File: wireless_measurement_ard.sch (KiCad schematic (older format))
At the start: 22 parts, among them J1 Conn_01x08, SW1 SW_SPDT, U2 JDY-08, U3 MCP16415, U4 MAX9938, U5 MAX9938, U6 EFM8LB1x-QFP32

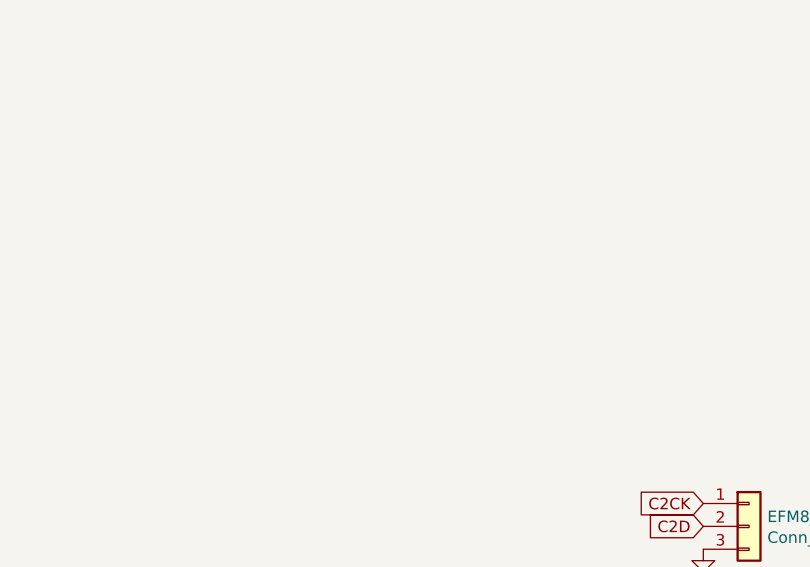
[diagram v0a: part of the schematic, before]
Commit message: update kicad to include holes
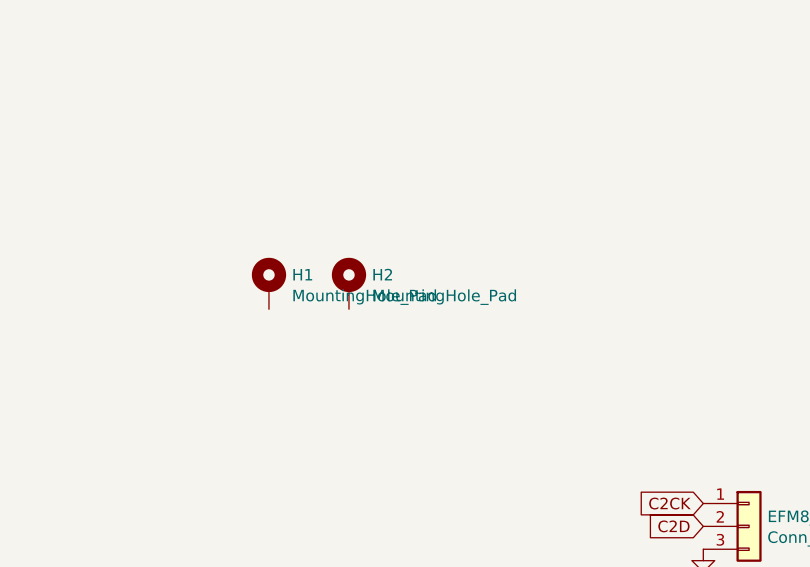
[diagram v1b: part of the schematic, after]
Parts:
- added H1, H2: MountingHole_Pad, MountingHole:MountingHole_2.2mm_M2_ISO7380_Pad, symbol Mechanical:MountingHole_Pad
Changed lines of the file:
@@
 Text GLabel 6200 4650 0    50   Input ~ 0
 VIN
+$Comp
+L Mechanical:MountingHole_Pad H1
+U 1 1 6108948B
+P 5550 2350
+F 0 "H1" H 5650 2399 50  0000 L CNN
+F 1 "MountingHole_Pad" H 5650 2308 50  0000 L CNN
+F 2 "MountingHole:MountingHole_2.2mm_M2_ISO7380_Pad" H 5550 2350 50  0001 C CNN
+F 3 "~" H 5550 2350 50  0001 C CNN
+	1    5550 2350
+	1    0    0    -1
+$EndComp
+$Comp
+L Mechanical:MountingHole_Pad H2
+U 1 1 61089F2F
+P 5900 2350
+F 0 "H2" H 6000 2399 50  0000 L CNN
+F 1 "MountingHole_Pad" H 6000 2308 50  0000 L CNN
+F 2 "MountingHole:MountingHole_2.2mm_M2_ISO7380_Pad" H 5900 2350 50  0001 C CNN
+F 3 "~" H 5900 2350 50  0001 C CNN
+	1    5900 2350
+	1    0    0    -1
+$EndComp
 $EndSCHEMATC

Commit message: update to fix VIO
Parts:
- added U1: EFM8LB1, Package_DFN_QFN:QFN-32-1EP_4x4mm_P0.4mm_EP2.9x2.9mm, symbol MCU_SiliconLabs:EFM8LB1
- U2: symbol jdy-08:JDY-08 -> wireless_measurement_ard-rescue:JDY-08-jdy-08
- U3: symbol gen_lib:MCP16415 -> wireless_measurement_ard-rescue:MCP16415-gen_lib
- U4, U5: symbol gen_lib:MAX9938 -> wireless_measurement_ard-rescue:MAX9938-gen_lib
- U6: symbol gen_lib:EFM8LB1x-QFP32 -> wireless_measurement_ard-rescue:EFM8LB1x-QFP32-gen_lib
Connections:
- net +3V3: now also U1.2 (VIO), U1.3 (VDD)
- net A0: now also U1.18 (P1.7)
- net A1: now also U1.19 (P1.6)
- net A2: now also U1.20 (P1.5)
- net A3: now also U1.21 (P1.4)
- net ARD_RX: now also U1.28 (P0.5)
- net ARD_TX: now also U1.29 (P0.4)
- net C2CK: now also U1.4 (RSTb/C2CK)
- net C2D: now also U1.5 (P3.7/C2D)
- net GND: now also U1.33 (GND)
- net PWRC: now also U1.23 (P1.2)
- net STATUS: now also U1.22 (P1.3)
- net LED: now reaches D1.2 (A), U6.25 (P1.0)
- net LED: now also U1.25 (P1.0)
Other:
- moved on the sheet: D1, R3
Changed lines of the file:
@@
 $EndDescr
 $Comp
-L jdy-08:JDY-08 U2
+L wireless_measurement_ard-rescue:JDY-08-jdy-08 U2
 U 1 1 60F6CD69
 P 3150 2100
@@
 $EndComp
 $Comp
-L gen_lib:MCP16415 U3
+L wireless_measurement_ard-rescue:MCP16415-gen_lib U3
 U 1 1 60F711CF
 P 9350 4500
@@
 $EndComp
 $Comp
-L gen_lib:MAX9938 U4
+L wireless_measurement_ard-rescue:MAX9938-gen_lib U4
 U 1 1 60F745CE
 P 8900 1750
@@
 $EndComp
 $Comp
-L gen_lib:MAX9938 U5
+L wireless_measurement_ard-rescue:MAX9938-gen_lib U5
 U 1 1 60F75707
 P 8900 2300
@@
 $EndComp
 $Comp
-L gen_lib:EFM8LB1x-QFP32 U6
+L wireless_measurement_ard-rescue:EFM8LB1x-QFP32-gen_lib U6
 U 1 1 6100BE6A
 P 3150 4900
@@
 Wire Wire Line
 	8550 4450 8950 4450
-$Comp
-L Device:LED D1
-U 1 1 61017CC7
-P 3800 4800
-F 0 "D1" H 3800 4700 50  0000 C CNN
-F 1 "LED" H 3800 4900 50  0000 C CNN
-F 2 "LED_SMD:LED_0603_1608Metric" H 3800 4800 50  0001 C CNN
-F 3 "~" H 3800 4800 50  0001 C CNN
-	1    3800 4800
-	-1   0    0    1
-$EndComp
-$Comp
-L Device:R R3
-U 1 1 6101884F
-P 4100 4800
-F 0 "R3" V 4200 4750 50  0000 L CNN
-F 1 "1k" V 4000 4750 50  0000 L CNN
-F 2 "Resistor_SMD:R_0603_1608Metric_Pad1.05x0.95mm_HandSolder" V 4030 4800 50  0001 C CNN
-F 3 "~" H 4100 4800 50  0001 C CNN
-	1    4100 4800
-	0    -1   -1   0
-$EndComp
-$Comp
-L power:GND #PWR0104
-U 1 1 61019046
-P 4250 4800
-F 0 "#PWR0104" H 4250 4550 50  0001 C CNN
-F 1 "GND" H 4255 4627 50  0000 C CNN
-F 2 "" H 4250 4800 50  0001 C CNN
-F 3 "" H 4250 4800 50  0001 C CNN
-	1    4250 4800
-	0    -1   -1   0
-$EndComp
 Text GLabel 3650 5000 2    50   Input ~ 0
 PWRC
@@
 	1    0    0    -1
 $EndComp
+$Comp
+L MCU_SiliconLabs:EFM8LB1 U1
+U 1 1 611E9E7B
+P 5100 5900
+F 0 "U1" H 5100 6915 50  0000 C CNN
+F 1 "EFM8LB1" H 5100 6824 50  0000 C CNN
+F 2 "Package_DFN_QFN:QFN-32-1EP_4x4mm_P0.4mm_EP2.9x2.9mm" H 5150 6100 50  0001 C CNN
+F 3 "" H 5150 6100 50  0001 C CNN
+	1    5100 5900
+	1    0    0    -1
+$EndComp
+Text GLabel 5700 5450 2    50   Input ~ 0
+ARD_TX
+Text GLabel 5700 5550 2    50   Input ~ 0
+ARD_RX
+$Comp
+L power:GND #PWR0108
+U 1 1 611EDCB4
+P 5100 6900
+F 0 "#PWR0108" H 5100 6650 50  0001 C CNN
+F 1 "GND" H 5105 6727 50  0000 C CNN
+F 2 "" H 5100 6900 50  0001 C CNN
+F 3 "" H 5100 6900 50  0001 C CNN
+	1    5100 6900
+	1    0    0    -1
+$EndComp
+$Comp
+L power:+3.3V #PWR0109
+U 1 1 611EE56A
+P 4500 5250
+F 0 "#PWR0109" H 4500 5100 50  0001 C CNN
+F 1 "+3.3V" H 4515 5423 50  0000 C CNN
+F 2 "" H 4500 5250 50  0001 C CNN
+F 3 "" H 4500 5250 50  0001 C CNN
+	1    4500 5250
+	0    -1   -1   0
+$EndComp
+$Comp
+L power:+3.3V #PWR0110
+U 1 1 611EF11F
+P 4500 5350
+F 0 "#PWR0110" H 4500 5200 50  0001 C CNN
+F 1 "+3.3V" H 4515 5523 50  0000 C CNN
+F 2 "" H 4500 5350 50  0001 C CNN
+F 3 "" H 4500 5350 50  0001 C CNN
+	1    4500 5350
+	0    -1   -1   0
+$EndComp
+Text GLabel 4500 5450 0    50   Input ~ 0
+C2CK
+Text GLabel 4500 5550 0    50   Input ~ 0
+C2D
+Text GLabel 5700 6050 2    50   Input ~ 0
+PWRC
+Text GLabel 5700 6150 2    50   Input ~ 0
+STATUS
+Text GLabel 5700 6250 2    50   Input ~ 0
+A3
+Text GLabel 5700 6350 2    50   Input ~ 0
+A2
+Text GLabel 5700 6450 2    50   Input ~ 0
+A1
+$Comp
+L power:GND #PWR0104
+U 1 1 61019046
+P 6500 3850
+F 0 "#PWR0104" H 6500 3600 50  0001 C CNN
+F 1 "GND" H 6505 3677 50  0000 C CNN
+F 2 "" H 6500 3850 50  0001 C CNN
+F 3 "" H 6500 3850 50  0001 C CNN
+	1    6500 3850
+	0    -1   -1   0
+$EndComp
+$Comp
+L Device:R R3
+U 1 1 6101884F
+P 6350 3850
+F 0 "R3" V 6450 3800 50  0000 L CNN
+F 1 "1k" V 6250 3800 50  0000 L CNN
+F 2 "Resistor_SMD:R_0603_1608Metric_Pad1.05x0.95mm_HandSolder" V 6280 3850 50  0001 C CNN
+F 3 "~" H 6350 3850 50  0001 C CNN
+	1    6350 3850
+	0    -1   -1   0
+$EndComp
+$Comp
+L Device:LED D1
+U 1 1 61017CC7
+P 6050 3850
+F 0 "D1" H 6050 3750 50  0000 C CNN
+F 1 "LED" H 6050 3950 50  0000 C CNN
+F 2 "LED_SMD:LED_0603_1608Metric" H 6050 3850 50  0001 C CNN
+F 3 "~" H 6050 3850 50  0001 C CNN
+	1    6050 3850
+	-1   0    0    1
+$EndComp
+Text GLabel 5900 3850 0    50   Input ~ 0
+LED
+Text GLabel 3650 4800 2    50   Input ~ 0
+LED
+Text GLabel 5700 5850 2    50   Input ~ 0
+LED
+Text GLabel 5700 6550 2    50   Input ~ 0
+A0
 $EndSCHEMATC

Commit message: updated footprint
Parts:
- removed U4: MAX9938, Package_TO_SOT_SMD:SOT-23-5_HandSoldering, symbol wireless_measurement_ard-rescue:MAX9938-gen_lib
- added C7: 4.7uF, Capacitor_SMD:C_0603_1608Metric_Pad1.08x0.95mm_HandSolder, symbol Device:C
- added R6: 1k, Resistor_SMD:R_0603_1608Metric_Pad0.98x0.95mm_HandSolder, symbol Device:R
- added U4: MAX44284, Package_TO_SOT_SMD:SOT-23-6_Handsoldering, symbol ben_common:MAX44284
- R2: value 5R3 -> 1R; footprint Resistor_SMD:R_0805_2012Metric_Pad1.15x1.40mm_HandSolder -> Resistor_SMD:R_0805_2012Metric_Pad1.20x1.40mm_HandSolder
- U1: symbol MCU_SiliconLabs:EFM8LB1 -> wireless_measurement_ard-rescue:EFM8LB1-MCU_SiliconLabs
- U2: symbol wireless_measurement_ard-rescue:JDY-08-jdy-08 -> wireless_measurement_ard-rescue:JDY-08-jdy-08-wireless_measurement_ard-rescue
- U3: symbol wireless_measurement_ard-rescue:MCP16415-gen_lib -> wireless_measurement_ard-rescue:MCP16415-gen_lib-wireless_measurement_ard-rescue
- U5: symbol wireless_measurement_ard-rescue:MAX9938-gen_lib -> wireless_measurement_ard-rescue:MAX9938-gen_lib-wireless_measurement_ard-rescue
- U6: symbol wireless_measurement_ard-rescue:EFM8LB1x-QFP32-gen_lib -> wireless_measurement_ard-rescue:EFM8LB1x-QFP32-gen_lib-wireless_measurement_ard-rescue
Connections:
- net +3V3: now also R6.1, U4.1 (VDD), U4.6 (!SHDN)
- net A0: now also U4.5 (OUT)
- net C1_IN: now also J1.2 (Pin_2), R2.2, U4.3 (RS+); no longer J1.1 (Pin_1), R2.1
- net C1_OUT: now also J1.1 (Pin_1), R2.1, U4.4 (RS-); no longer J1.2 (Pin_2), R2.2
- net C2CK: now also R6.2
- net GND: now also C7.1, U4.2 (GND)
- net P0.0: now reaches U6.1 (P0.0)
- net P0.0: now also U1.1 (P0.0), C7.2
- net P3.0: now reaches U6.10 (P3.0)
- net P3.0: now also U1.10 (P3.0)
- net P2.6: now reaches U6.11 (P2.6)
- net P2.6: now also U1.11 (P2.6)
- net P2.5: now reaches U6.12 (P2.5)
- net P2.5: now also U1.12 (P2.5)
- net P2.4: now reaches U6.13 (P2.4)
- net P2.4: now also U1.13 (P2.4)
- net P2.3: now reaches U6.14 (P2.3)
- net P2.3: now also U1.14 (P2.3)
- net P2.2: now reaches U6.15 (P2.2)
- net P2.2: now also U1.15 (P2.2)
- net P2.1: now reaches U6.16 (P2.1)
- net P2.1: now also U1.16 (P2.1)
- net P2.0: now reaches U6.17 (P2.0)
- net P2.0: now also U1.17 (P2.0)
- net P1.1: now reaches U6.24 (P1.1)
- net P1.1: now also U1.24 (P1.1)
- net P0.7: now reaches U6.26 (P0.7)
- net P0.7: now also U1.26 (P0.7)
- net P0.6: now reaches U6.27 (P0.6)
- net P0.6: now also U1.27 (P0.6)
- net P0.3: now reaches U6.30 (P0.3)
- net P0.3: now also U1.30 (P0.3)
- net P0.2: now reaches U6.31 (P0.2)
- net P0.2: now also U1.31 (P0.2)
- net P0.1: now reaches U6.32 (P0.1)
- net P0.1: now also U1.32 (P0.1)
- net P3.3: now reaches U6.7 (P3.3)
- net P3.3: now also U1.7 (P3.3)
- net P3.2: now reaches U6.8 (P3.2)
- net P3.2: now also U1.8 (P3.2)
- net P3.1: now reaches U6.9 (P3.1)
- net P3.1: now also U1.9 (P3.1)
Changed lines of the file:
@@
 $EndDescr
 $Comp
-L wireless_measurement_ard-rescue:JDY-08-jdy-08 U2
+L wireless_measurement_ard-rescue:JDY-08-jdy-08-wireless_measurement_ard-rescue U2
 U 1 1 60F6CD69
 P 3150 2100
@@
 $EndComp
 $Comp
-L wireless_measurement_ard-rescue:MCP16415-gen_lib U3
+L wireless_measurement_ard-rescue:MCP16415-gen_lib-wireless_measurement_ard-rescue U3
 U 1 1 60F711CF
 P 9350 4500
@@
 $EndComp
 $Comp
-L wireless_measurement_ard-rescue:MAX9938-gen_lib U4
-U 1 1 60F745CE
-P 8900 1750
-F 0 "U4" H 8900 2065 50  0000 C CNN
-F 1 "MAX9938" H 8900 1974 50  0000 C CNN
-F 2 "Package_TO_SOT_SMD:SOT-23-5_HandSoldering" H 8900 1450 50  0001 C CNN
-F 3 "http://www.farnell.com/datasheets/2345095.pdf" H 8900 1750 50  0001 C CNN
-	1    8900 1750
-	1    0    0    -1
-$EndComp
-$Comp
-L wireless_measurement_ard-rescue:MAX9938-gen_lib U5
+L wireless_measurement_ard-rescue:MAX9938-gen_lib-wireless_measurement_ard-rescue U5
 U 1 1 60F75707
 P 8900 2300
@@
 F 3 "http://www.farnell.com/datasheets/2345095.pdf" H 8900 2300 50  0001 C CNN
 	1    8900 2300
-	1    0    0    -1
-$EndComp
-$Comp
-L power:GND #PWR0101
-U 1 1 60F7603A
-P 8550 1850
-F 0 "#PWR0101" H 8550 1600 50  0001 C CNN
-F 1 "GND" H 8555 1677 50  0000 C CNN
-F 2 "" H 8550 1850 50  0001 C CNN
-F 3 "" H 8550 1850 50  0001 C CNN
-	1    8550 1850
 	1    0    0    -1
 $EndComp
@@
 Wire Wire Line
 	8550 2200 8400 2200
-Wire Wire Line
-	8550 1650 8400 1650
-Text GLabel 8400 1650 0    50   Input ~ 0
-A0
 Text GLabel 8400 2200 0    50   Input ~ 0
 A1
-Wire Wire Line
-	9250 1650 9350 1650
-Wire Wire Line
-	9350 1650 9350 1550
-Wire Wire Line
-	9250 1750 9350 1750
-Wire Wire Line
-	9350 1750 9350 1850
 Wire Wire Line
 	9250 2200 9250 2100
@@
 	1    0    0    -1
 $EndComp
-Connection ~ 9450 1550
-Connection ~ 9450 1850
-Wire Wire Line
-	9450 1850 9650 1850
-Wire Wire Line
-	9350 1850 9450 1850
-Wire Wire Line
-	9450 1550 9650 1550
-Wire Wire Line
-	9350 1550 9450 1550
-$Comp
-L Device:R R2
-U 1 1 60F77736
-P 9450 1700
-F 0 "R2" H 9520 1746 50  0000 L CNN
-F 1 "5R3" H 9520 1655 50  0000 L CNN
-F 2 "Resistor_SMD:R_0805_2012Metric_Pad1.15x1.40mm_HandSolder" V 9380 1700 50  0001 C CNN
-F 3 "~" H 9450 1700 50  0001 C CNN
-	1    9450 1700
-	1    0    0    -1
-$EndComp
 Wire Wire Line
 	9650 2100 9650 2200
 Wire Wire Line
 	9650 2300 9650 2400
-Wire Wire Line
-	9650 1850 9650 1750
-Wire Wire Line
-	9650 1650 9650 1550
 Text Notes 8950 1150 0    50   ~ 0
 uA current sensing
@@
 Wire Wire Line
 	9150 3500 9300 3500
-Text GLabel 9800 1650 2    50   Input ~ 0
-C1_IN
 Text GLabel 9800 2300 2    50   Input ~ 0
 C2_OUT
@@
 Wire Wire Line
 	9650 2300 9800 2300
-Wire Wire Line
-	9650 1750 9800 1750
-Wire Wire Line
-	9650 1650 9800 1650
+Text GLabel 9300 2900 0    50   Input ~ 0
+C1_IN
 Text GLabel 9300 2800 0    50   Input ~ 0
-C1_IN
-Text GLabel 9800 1750 2    50   Input ~ 0
-C1_OUT
-Text GLabel 9300 2900 0    50   Input ~ 0
 C1_OUT
 Text GLabel 9300 3000 0    50   Input ~ 0
@@
 $EndComp
 Wire Wire Line
-	8550 1750 8550 1850
-Connection ~ 8550 1850
-Wire Wire Line
 	8550 2300 8550 2400
 Connection ~ 8550 2400
@@
 $EndComp
 $Comp
-L wireless_measurement_ard-rescue:EFM8LB1x-QFP32-gen_lib U6
+L wireless_measurement_ard-rescue:EFM8LB1x-QFP32-gen_lib-wireless_measurement_ard-rescue U6
 U 1 1 6100BE6A
 P 3150 4900
@@
 L power:GND #PWR0120
 U 1 1 61018C99
-P 2650 4200
-F 0 "#PWR0120" H 2650 3950 50  0001 C CNN
-F 1 "GND" H 2655 4027 50  0000 C CNN
-F 2 "" H 2650 4200 50  0001 C CNN
-F 3 "" H 2650 4200 50  0001 C CNN
-	1    2650 4200
+P 2300 4200
+F 0 "#PWR0120" H 2300 3950 50  0001 C CNN
+F 1 "GND" H 2305 4027 50  0000 C CNN
+F 2 "" H 2300 4200 50  0001 C CNN
+F 3 "" H 2300 4200 50  0001 C CNN
+	1    2300 4200
 	0    1    1    0
 $EndComp
@@
 Text GLabel 7450 3400 0    50   Input ~ 0
 C2D
-Text GLabel 7450 3300 0    50   Input ~ 0
+Text GLabel 7150 3300 0    50   Input ~ 0
 C2CK
 Wire Wire Line
@@
 $EndComp
 $Comp
-L MCU_SiliconLabs:EFM8LB1 U1
+L wireless_measurement_ard-rescue:EFM8LB1-MCU_SiliconLabs U1
 U 1 1 611E9E7B
 P 5100 5900
@@
 Text GLabel 5700 6550 2    50   Input ~ 0
 A0
+$Comp
+L Device:C C7
+U 1 1 614EE1A5
+P 2350 3950
+F 0 "C7" H 2100 4000 50  0000 L CNN
+F 1 "4.7uF" H 2050 3900 50  0000 L CNN
+F 2 "Capacitor_SMD:C_0603_1608Metric_Pad1.08x0.95mm_HandSolder" H 2388 3800 50  0001 C CNN
+F 3 "~" H 2350 3950 50  0001 C CNN
+	1    2350 3950
+	-1   0    0    1
+$EndComp
+Wire Wire Line
+	2350 4100 2350 4200
+Wire Wire Line
+	2350 4200 2300 4200
+Wire Wire Line
+	2650 4200 2350 4200
+Connection ~ 2350 4200
+$Comp
+L Device:R R6
+U 1 1 614F21C7
+P 7300 3150
+F 0 "R6" V 7400 3100 50  0000 L CNN
+F 1 "1k" V 7200 3100 50  0000 L CNN
+F 2 "Resistor_SMD:R_0603_1608Metric_Pad0.98x0.95mm_HandSolder" V 7230 3150 50  0001 C CNN
+F 3 "~" H 7300 3150 50  0001 C CNN
+	1    7300 3150
+	1    0    0    -1
+$EndComp
+$Comp
+L power:+3.3V #PWR0111
+U 1 1 614F2925
+P 7300 3000
+F 0 "#PWR0111" H 7300 2850 50  0001 C CNN
+F 1 "+3.3V" H 7315 3173 50  0000 C CNN
+F 2 "" H 7300 3000 50  0001 C CNN
+F 3 "" H 7300 3000 50  0001 C CNN
+	1    7300 3000
+	1    0    0    -1
+$EndComp
+Wire Wire Line
+	7150 3300 7300 3300
+Connection ~ 7300 3300
+Wire Wire Line
+	7300 3300 7450 3300
+Text GLabel 3650 4900 2    50   Input ~ 0
+P1.1
+Text GLabel 3650 4700 2    50   Input ~ 0
+P0.7
+Text GLabel 3650 4600 2    50   Input ~ 0
+P0.6
+Text GLabel 3650 4300 2    50   Input ~ 0
+P0.3
+Text GLabel 3650 4100 2    50   Input ~ 0
+P0.1
+Text GLabel 3650 4200 2    50   Input ~ 0
+P0.2
+Text GLabel 3650 5600 2    50   Input ~ 0
+P2.0
+Text GLabel 2650 5600 0    50   Input ~ 0
+P2.1
+Text GLabel 2650 5500 0    50   Input ~ 0
+P2.2
+Text GLabel 2650 5400 0    50   Input ~ 0
+P2.3
+Text GLabel 2650 5300 0    50   Input ~ 0
+P2.4
+Text GLabel 2650 5200 0    50   Input ~ 0
+P2.5
+Text GLabel 2650 5100 0    50   Input ~ 0
+P2.6
+Text GLabel 2650 5000 0    50   Input ~ 0
+P3.0
+Text GLabel 2650 4900 0    50   Input ~ 0
+P3.1
+Text GLabel 2650 4800 0    50   Input ~ 0
+P3.2
+Text GLabel 2650 4700 0    50   Input ~ 0
+P3.3
+Text GLabel 2650 4100 0    50   Input ~ 0
+P0.0
+Text GLabel 2350 3800 0    50   Input ~ 0
+P0.0
+Text GLabel 4500 6650 0    50   Input ~ 0
+P2.1
+Text GLabel 4500 6550 0    50   Input ~ 0
+P2.2
+Text GLabel 4500 6450 0    50   Input ~ 0
+P2.3
+Text GLabel 4500 6350 0    50   Input ~ 0
+P2.4
+Text GLabel 4500 6250 0    50   Input ~ 0
+P2.5
+Text GLabel 4500 6150 0    50   Input ~ 0
+P2.6
+Text GLabel 4500 6050 0    50   Input ~ 0
+P3.0
+Text GLabel 4500 5950 0    50   Input ~ 0
+P3.1
+Text GLabel 4500 5850 0    50   Input ~ 0
+P3.2
+Text GLabel 4500 5750 0    50   Input ~ 0
+P3.3
+Text GLabel 5700 5650 2    50   Input ~ 0
+P0.6
+Text GLabel 5700 5750 2    50   Input ~ 0
+P0.7
+Text GLabel 5700 5950 2    50   Input ~ 0
+P1.1
+Text GLabel 5700 6650 2    50   Input ~ 0
+P2.0
+Text GLabel 5700 5350 2    50   Input ~ 0
+P0.3
+Text GLabel 5700 5150 2    50   Input ~ 0
+P0.1
+Text GLabel 5700 5250 2    50   Input ~ 0
+P0.2
+Text GLabel 4500 5150 0    50   Input ~ 0
+P0.0
+$Comp
+L ben_common:MAX44284 U4
+U 1 1 61508E2E
+P 8800 1650
+F 0 "U4" H 8800 1975 50  0000 C CNN
+F 1 "MAX44284" H 8800 1884 50  0000 C CNN
+F 2 "Package_TO_SOT_SMD:SOT-23-6_Handsoldering" H 8800 1450 50  0001 C CNN
+F 3 "https://datasheets.maximintegrated.com/en/ds/MAX44284.pdf" H 8800 1450 50  0001 C CNN
+	1    8800 1650
+	1    0    0    -1
+$EndComp
+Text GLabel 9150 1550 2    50   Input ~ 0
+A0
+$Comp
+L power:GND #PWR0101
+U 1 1 61509478
+P 8300 1750
+F 0 "#PWR0101" H 8300 1500 50  0001 C CNN
+F 1 "GND" H 8305 1577 50  0000 C CNN
+F 2 "" H 8300 1750 50  0001 C CNN
+F 3 "" H 8300 1750 50  0001 C CNN
+	1    8300 1750
+	1    0    0    -1
+$EndComp
+Wire Wire Line
+	8450 1750 8300 1750
+$Comp
+L power:+3.3V #PWR0122
+U 1 1 6150FCA8
+P 8200 1650
+F 0 "#PWR0122" H 8200 1500 50  0001 C CNN
+F 1 "+3.3V" H 8215 1823 50  0000 C CNN
+F 2 "" H 8200 1650 50  0001 C CNN
+F 3 "" H 8200 1650 50  0001 C CNN
+	1    8200 1650
+	0    -1   -1   0
+$EndComp
+Wire Wire Line
+	8200 1650 8400 1650
+$Comp
+L Device:R R2
+U 1 1 615123F2
+P 9450 1700
+F 0 "R2" H 9520 1746 50  0000 L CNN
+F 1 "1R" H 9520 1655 50  0000 L CNN
+F 2 "Resistor_SMD:R_0805_2012Metric_Pad1.20x1.40mm_HandSolder" V 9380 1700 50  0001 C CNN
+F 3 "~" H 9450 1700 50  0001 C CNN
+	1    9450 1700
+	1    0    0    -1
+$EndComp
+Text GLabel 9800 1650 2    50   Input ~ 0
+C1_OUT
+Wire Wire Line
+	9650 1650 9800 1650
+Wire Wire Line
+	9650 1750 9800 1750
+Text GLabel 9800 1750 2    50   Input ~ 0
+C1_IN
+Wire Wire Line
+	9650 1650 9650 1550
+Wire Wire Line
+	9650 1850 9650 1750
+Wire Wire Line
+	9650 1550 9450 1550
+Wire Wire Line
+	9450 1550 9350 1550
+Wire Wire Line
+	9350 1550 9350 1650
+Wire Wire Line
+	9350 1650 9150 1650
+Connection ~ 9450 1550
+Wire Wire Line
+	9150 1750 9350 1750
+Wire Wire Line
+	9350 1750 9350 1850
+Wire Wire Line
+	9350 1850 9450 1850
+Connection ~ 9450 1850
+Wire Wire Line
+	9450 1850 9650 1850
+Wire Wire Line
+	8450 1550 8400 1550
+Wire Wire Line
+	8400 1550 8400 1650
+Connection ~ 8400 1650
+Wire Wire Line
+	8400 1650 8450 1650
 $EndSCHEMATC
